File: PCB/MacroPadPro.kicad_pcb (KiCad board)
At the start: 2 copper layers, 160.7 x 77.6 mm, 119 parts, among them J1 KXT331LHS, J2 KXT331LHS, SW1 CPG151101S11, SW10 CPG151101S11, SW11 CPG151101S11, SW12 CPG151101S11, SW13 CPG151101S11, SW14 CPG151101S11, SW15 CPG151101S11, SW16 CPG151101S11, SW17 CPG151101S11, SW18 CPG151101S11, SW19 CPG151101S11, SW2 CPG151101S11, SW20 CPG151101S11, SW21 CPG151101S11, SW22 CPG151101S11, SW23 CPG151101S11, SW24 CPG151101S11, SW25 CPG151101S11, SW26 CPG151101S11, SW27 CPG151101S11, SW3 CPG151101S11, SW4 CPG151101S11, SW5 CPG151101S11, SW6 CPG151101S11, SW7 CPG151101S11, SW8 CPG151101S11, SW9 CPG151101S11, U1 AP2210N-3.3TRG1, U3 RP2040, Y1 TAXM12M4RKDCDT2T

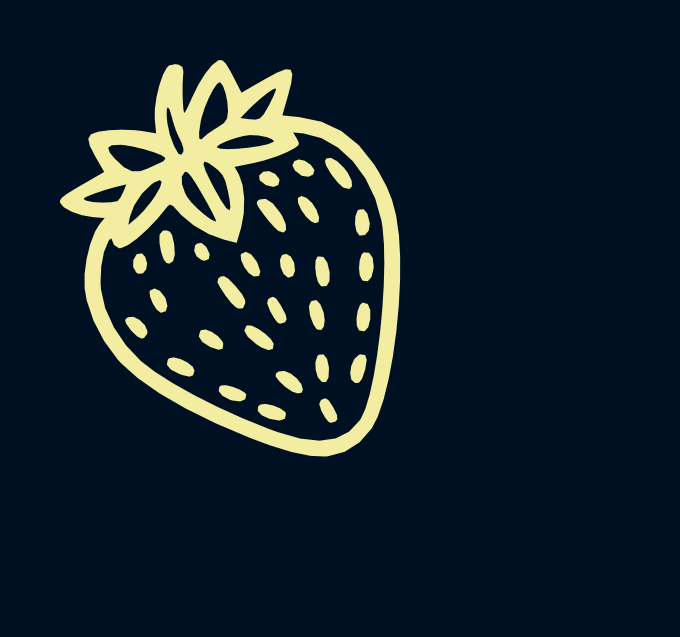
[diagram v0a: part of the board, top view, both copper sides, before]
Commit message: Updated BOM components, fixed with known working parts
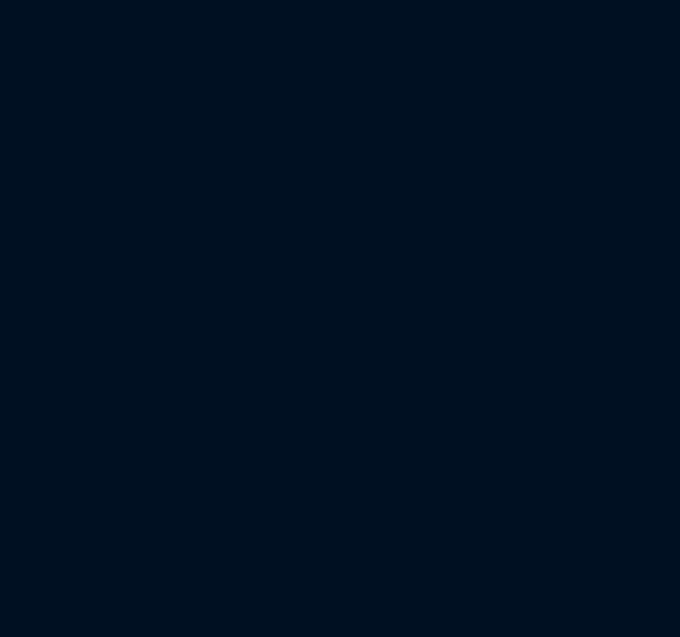
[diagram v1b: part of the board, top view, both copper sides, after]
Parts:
- removed the G*** at (28.5, -116.9)
- C1, C10, C3, C4: value GRT033R60J105ME13D -> JMK105BJ105KV-F
- C11, C13, C14, C15, C18, C5, C6, C7, C8: value CSA0201X5R104K6R3ET -> CC0402KRX5R5BB104
- R1, R7: value 0201WMF1001TEE -> CRT0402AFY-1001GLF
- R2: value 0201WMF1002TEE -> CRT0402ADY-1002GLF
- R3, R4: value 0201WMJ0270TEE -> CRG0402F27R
- R5, R6: value RTT01512JTH -> CR0402F5K10Q10Z
- USB2: value HRO-TYPE-C-31-M-12 -> TYPE-C-31-M-12
